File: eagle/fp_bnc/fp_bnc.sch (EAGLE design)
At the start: 12 parts, among them J1 031-5329-52RFX, J2 031-5329-52RFX, J5 TSM-110-01-S-SV

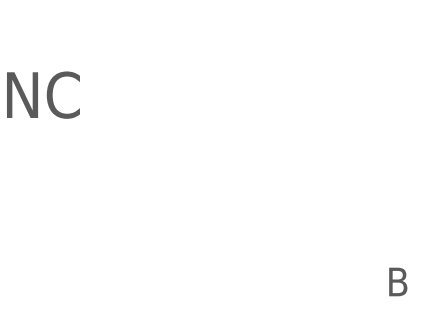
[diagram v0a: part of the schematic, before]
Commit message: Pre-production update.
* Increased clearances from chassis/enclosure ground.
* Improved text.
* Added gerbers.
* Added USB back panel.
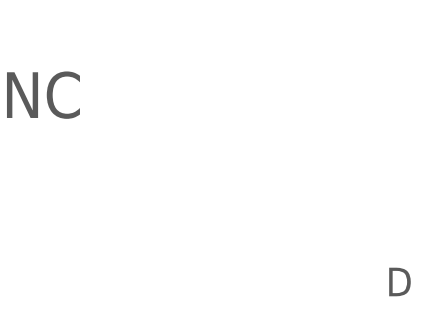
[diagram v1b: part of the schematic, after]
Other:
- note added: "D"
- note removed: "B"
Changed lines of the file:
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@@
 <?xml version="1.0" encoding="utf-8"?>
 <!DOCTYPE eagle SYSTEM "eagle.dtd">
-<eagle version="9.2.2">
+<eagle version="9.3.2">
 <drawing>
 <settings>
@@
 <grid distance="0.1" unitdist="inch" unit="inch" style="lines" multiple="1" display="no" altdistance="0.01" altunitdist="inch" altunit="inch"/>
 <layers>
-<layer number="1" name="Top" color="4" fill="1" visible="yes" active="no"/>
-<layer number="2" name="Route2" color="1" fill="3" visible="yes" active="no"/>
-<layer number="15" name="Route15" color="4" fill="6" visible="yes" active="no"/>
-<layer number="16" name="Bottom" color="1" fill="1" visible="yes" active="no"/>
-<layer number="17" name="Pads" color="2" fill="1" visible="yes" active="no"/>
-<layer number="18" name="Vias" color="2" fill="1" visible="yes" active="no"/>
-<layer number="19" name="Unrouted" color="6" fill="1" visible="yes" active="no"/>
-<layer number="20" name="Dimension" color="24" fill="1" visible="yes" active="no"/>
-<layer number="21" name="tPlace" color="7" fill="1" visible="yes" active="no"/>
-<layer number="22" name="bPlace" color="7" fill="1" visible="yes" active="no"/>
-<layer number="23" name="tOrigins" color="15" fill="1" visible="yes" active="no"/>
-<layer number="24" name="bOrigins" color="15" fill="1" visible="yes" active="no"/>
-<layer number="25" name="tNames" color="7" fill="1" visible="yes" active="no"/>
-<layer number="26" name="bNames" color="7" fill="1" visible="yes" active="no"/>
-<layer number="27" name="tValues" color="7" fill="1" visible="yes" active="no"/>
-<layer number="28" name="bValues" color="7" fill="1" visible="yes" active="no"/>
+<layer number="1" name="Top" color="4" fill="1" visible="no" active="no"/>
+<layer number="2" name="Route2" color="1" fill="3" visible="no" active="no"/>
+<layer number="15" name="Route15" color="4" fill="6" visible="no" active="no"/>
+<layer number="16" name="Bottom" color="1" fill="1" visible="no" active="no"/>
+<layer number="17" name="Pads" color="2" fill="1" visible="no" active="no"/>
+<layer number="18" name="Vias" color="2" fill="1" visible="no" active="no"/>
+<layer number="19" name="Unrouted" color="6" fill="1" visible="no" active="no"/>
+<layer number="20" name="Dimension" color="24" fill="1" visible="no" active="no"/>
+<layer number="21" name="tPlace" color="7" fill="1" visible="no" active="no"/>
+<layer number="22" name="bPlace" color="7" fill="1" visible="no" active="no"/>
+<layer number="23" name="tOrigins" color="15" fill="1" visible="no" active="no"/>
+<layer number="24" name="bOrigins" color="15" fill="1" visible="no" active="no"/>
+<layer number="25" name="tNames" color="7" fill="1" visible="no" active="no"/>
+<layer number="26" name="bNames" color="7" fill="1" visible="no" active="no"/>
+<layer number="27" name="tValues" color="7" fill="1" visible="no" active="no"/>
+<layer number="28" name="bValues" color="7" fill="1" visible="no" active="no"/>
 <layer number="29" name="tStop" color="7" fill="3" visible="no" active="no"/>
 <layer number="30" name="bStop" color="7" fill="6" visible="no" active="no"/>
@@
 <layer number="35" name="tGlue" color="7" fill="4" visible="no" active="no"/>
 <layer number="36" name="bGlue" color="7" fill="5" visible="no" active="no"/>
-<layer number="37" name="tTest" color="7" fill="1" visible="yes" active="no"/>
-<layer number="38" name="bTest" color="7" fill="1" visible="yes" active="no"/>
+<layer number="37" name="tTest" color="7" fill="1" visible="no" active="no"/>
+<layer number="38" name="bTest" color="7" fill="1" visible="no" active="no"/>
 <layer number="39" name="tKeepout" color="4" fill="11" visible="no" active="no"/>
 <layer number="40" name="bKeepout" color="1" fill="11" visible="no" active="no"/>
@@
 <layer number="44" name="Drills" color="7" fill="1" visible="no" active="no"/>
 <layer number="45" name="Holes" color="7" fill="1" visible="no" active="no"/>
-<layer number="46" name="Milling" color="3" fill="1" visible="yes" active="no"/>
-<layer number="47" name="Measures" color="7" fill="1" visible="yes" active="no"/>
-<layer number="48" name="Document" color="7" fill="1" visible="yes" active="no"/>
-<layer number="49" name="Reference" color="7" fill="1" visible="yes" active="no"/>
-<layer number="50" name="dxf" color="7" fill="1" visible="yes" active="no"/>
-<layer number="51" name="tDocu" color="7" fill="1" visible="yes" active="no"/>
-<layer number="52" name="bDocu" color="7" fill="1" visible="yes" active="no"/>
-<layer number="53" name="tGND_GNDA" color="7" fill="9" visible="yes" active="no"/>
-<layer number="54" name="bGND_GNDA" color="1" fill="9" visible="yes" active="no"/>
-<layer number="56" name="wert" color="7" fill="1" visible="yes" active="no"/>
-<layer number="57" name="tCAD" color="7" fill="1" visible="yes" active="no"/>
-<layer number="59" name="tCarbon" color="7" fill="1" visible="yes" active="no"/>
-<layer number="60" name="bCarbon" color="7" fill="1" visible="yes" active="no"/>
+<layer number="46" name="Milling" color="3" fill="1" visible="no" active="no"/>
+<layer number="47" name="Measures" color="7" fill="1" visible="no" active="no"/>
+<layer number="48" name="Document" color="7" fill="1" visible="no" active="no"/>
+<layer number="49" name="Reference" color="7" fill="1" visible="no" active="no"/>
+<layer number="50" name="dxf" color="7" fill="1" visible="no" active="no"/>
+<layer number="51" name="tDocu" color="7" fill="1" visible="no" active="no"/>
+<layer number="52" name="bDocu" color="7" fill="1" visible="no" active="no"/>
+<layer number="53" name="tGND_GNDA" color="7" fill="9" visible="no" active="no"/>
+<layer number="54" name="bGND_GNDA" color="1" fill="9" visible="no" active="no"/>
+<layer number="56" name="wert" color="7" fill="1" visible="no" active="no"/>
+<layer number="57" name="tCAD" color="7" fill="1" visible="no" active="no"/>
+<layer number="59" name="tCarbon" color="7" fill="1" visible="no" active="no"/>
+<layer number="60" name="bCarbon" color="7" fill="1" visible="no" active="no"/>
 <layer number="88" name="SimResults" color="9" fill="1" visible="yes" active="yes"/>
 <layer number="89" name="SimProbes" color="9" fill="1" visible="yes" active="yes"/>
@@
 <plain>
 <text x="177.8" y="26.162" size="5.08" layer="97">Front Panel - BNC</text>
-<text x="266.7" y="6.35" size="3.175" layer="97">B</text>
+<text x="266.7" y="6.35" size="3.175" layer="97">D</text>
 <text x="99.06" y="205.74" size="2.54" layer="97" align="center">IN</text>
 <text x="165.1" y="205.74" size="2.54" layer="97" align="center">OUT</text>
